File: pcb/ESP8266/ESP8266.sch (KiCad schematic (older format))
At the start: 18 parts, among them J1 Conn_02x04, U1 ESP8266EX, U2 W25Q16BVSSIG

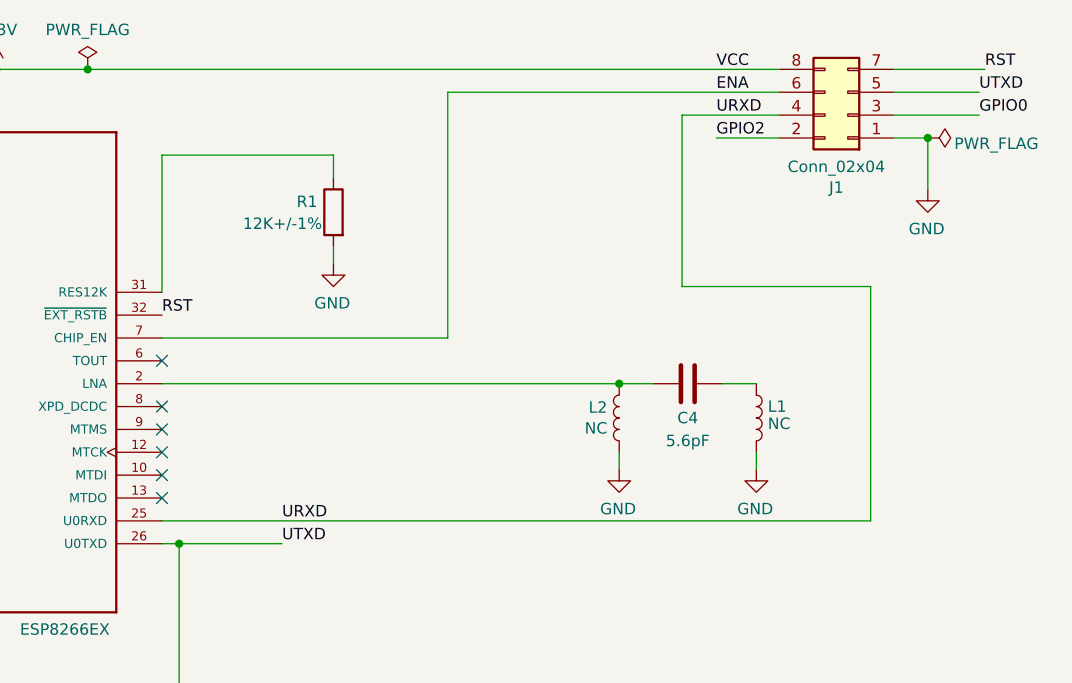
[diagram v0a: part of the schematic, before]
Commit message: cambio de footprint en las resistencias y capacitores, fin de pcb V1.0
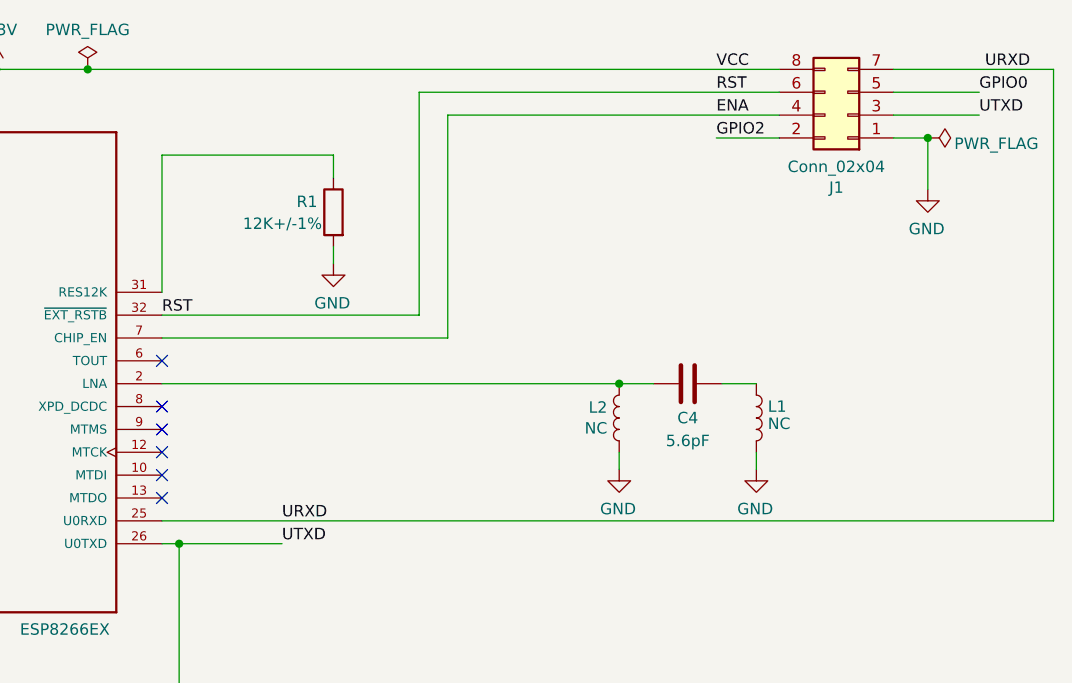
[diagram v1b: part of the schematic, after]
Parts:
- C1, C2, C3, C4: footprint Capacitor_SMD:C_0201_0603Metric -> Capacitor_SMD:C_0402_1005Metric
- D1, D2, R1, R2, R3, R4, R5: footprint Resistor_SMD:R_0201_0603Metric -> Resistor_SMD:R_0402_1005Metric
- J1: footprint Connector_Molex:Molex_Micro-Fit_3.0_43045-0812_2x04_P3.00mm_Vertical -> Connector_PinHeader_1.27mm:PinHeader_2x04_P1.27mm_Vertical
- L1, L2: footprint Inductor_SMD:L_0201_0603Metric -> Inductor_SMD:L_0402_1005Metric
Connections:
- net ENA: now also J1.4 (Pin_4); no longer J1.6 (Pin_6)
- net GPIO0: now also J1.5 (Pin_5); no longer J1.3 (Pin_3)
- net RST: now also J1.6 (Pin_6); no longer J1.7 (Pin_7)
- net URXD: now also J1.7 (Pin_7); no longer J1.4 (Pin_4)
- net UTXD: now also J1.3 (Pin_3); no longer J1.5 (Pin_5)
